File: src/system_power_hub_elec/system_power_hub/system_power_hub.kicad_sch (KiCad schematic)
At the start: 43 parts, among them J101 SM02B-PASS, J6 IDC6, U102 TCAN1462V, U2 STM32G474RBT6, U4 24LC128, Y1 24MHz

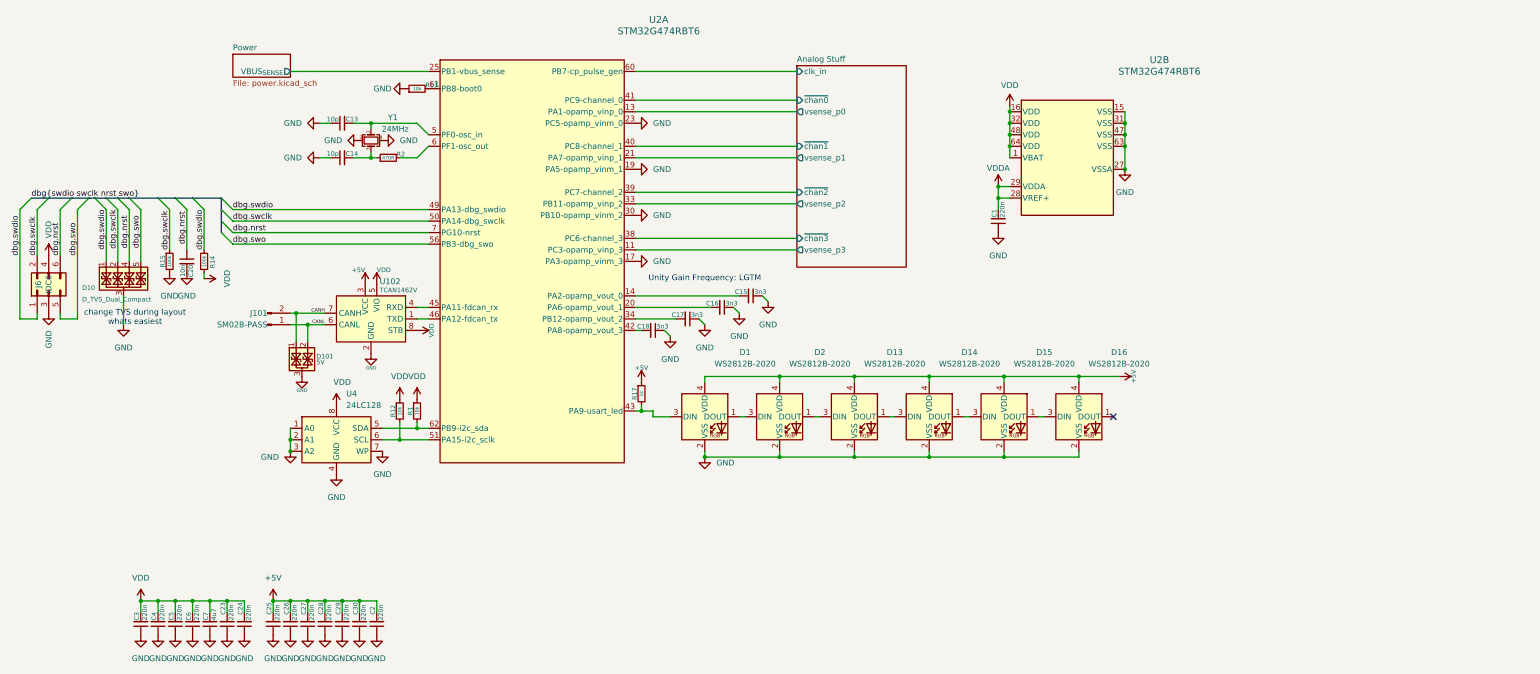
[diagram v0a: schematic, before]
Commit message: [WIP] Copied KiCAD proj from MPM, modified schematic for SPM
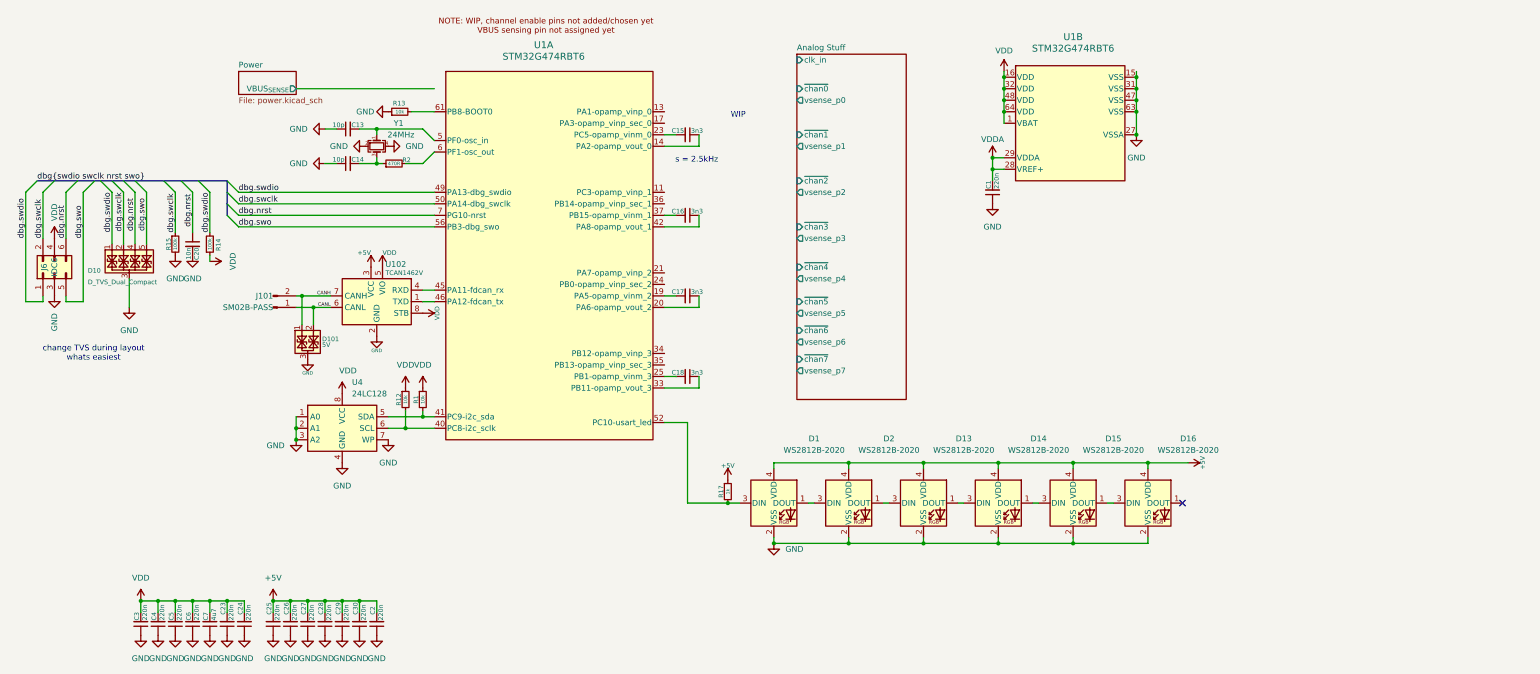
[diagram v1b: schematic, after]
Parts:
- removed U2: STM32G474RBT6, Package_QFP:LQFP-64_10x10mm_P0.5mm, symbol Main_Power_Module:STM32G474RBT6
- added U1: STM32G474RBT6, LQFP64-10x10mm, symbol CubeMX:STM32G474RBT6
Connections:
- net GND: now also U1.15 (VSS), U1.27 (VSSA), U1.31 (VSS), U1.47 (VSS), U1.63 (VSS); no longer C15.1, C16.1, C17.1, C18.1
- net VDD: now also U1.1 (VBAT), U1.16 (VDD), U1.32 (VDD), U1.48 (VDD), U1.64 (VDD)
- net VDDA: now also U1.28 (VREF+), U1.29 (VDDA)
- net dbg.nrst: now also U1.7 (PG10-nrst)
- net dbg.swclk: now also U1.50 (PA14-dbg_swclk)
- net dbg.swdio: now also U1.49 (PA13-dbg_swdio)
- net dbg.swo: now also U1.56 (PB3-dbg_swo)
- net at C15.2: now also U1.23 (PC5-opamp_vinm_0)
- net at C16.2: now also U1.37 (PB15-opamp_vinm_1)
- net at C17.2: now also U1.19 (PA5-opamp_vinm_2)
- net at C18.2: now also U1.25 (PB1-opamp_vinm_3)
- net at D1.3 (DIN), R17.2: now also U1.52 (PC10-usart_led)
- net at U102.4 (RXD): now also U1.45 (PA11-fdcan_rx)
- net at U102.1 (TXD): now also U1.46 (PA12-fdcan_tx)
- net at C13.2, Y1.1: now also U1.5 (PF0-osc_in)
- net at R12.2, U4.6 (SCL): now also U1.40 (PC8-i2c_sclk)
- net at R2.2: now also U1.6 (PF1-osc_out)
- net at R13.2: now also U1.61 (PB8-BOOT0)
- net at R1.2, U4.5 (SDA): now also U1.41 (PC9-i2c_sda)
- new net: C17.1, U1.20 (PA6-opamp_vout_2)
- new net: C15.1, U1.14 (PA2-opamp_vout_0)
- new net: C16.1, U1.42 (PA8-opamp_vout_1)
- new net: C18.1, U1.33 (PB11-opamp_vout_3)
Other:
- sheet Analog Stuff ports: added vsense_p4, vsense_p5, vsense_p6, vsense_p7, ~{chan4}, ~{chan5}, ~{chan6}, ~{chan7}; removed none
- note added: "WIP"
- note added: "s = 2.5kHz"
- note removed: "Unity Gain Frequency: LGTM"
- moved on the sheet: C1, C13, C14, C15, C16, C17, C18, C20, D1, D10, D101, D13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

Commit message: Draft SPM PCB layout
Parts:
- U1: footprint LQFP64-10x10mm -> Package_QFP:LQFP-64_10x10mm_P0.5mm
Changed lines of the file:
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@@
 			)
 		)
-		(property "Footprint" "LQFP64-10x10mm"
+		(property "Footprint" "Package_QFP:LQFP-64_10x10mm_P0.5mm"
 			(at 233.68 43.18 0)
 			(effects
@@
 			)
 		)
-		(property "Footprint" "LQFP64-10x10mm"
+		(property "Footprint" "Package_QFP:LQFP-64_10x10mm_P0.5mm"
 			(at 115.57 41.91 0)
 			(effects

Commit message: Draft layout done, need to continue routing and decide on GPIO
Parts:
- added C32, C33, C60, C61: 220n, Capacitor_SMD:C_0402_1005Metric, symbol Bluesat:C_CompactV
- added D4, D5, D6, D7: WS2812B-2020, LED_SMD:LED_WS2812B-2020_PLCC4_2.0x2.0mm, symbol LED:WS2812B-2020
- added H1, H2, H3, H4: MountingHole, Bluesat:M2.5, symbol Mechanical:MountingHole
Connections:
- net +5V: now also C32.2, C33.2, C60.2, C61.2, D4.4 (VDD), D5.4 (VDD), D6.4 (VDD), D7.4 (VDD)
- net GND: now also C32.1, C33.1, C60.1, C61.1, D4.2 (VSS), D5.2 (VSS), D6.2 (VSS), D7.2 (VSS)
- net at D16.1 (DOUT): now also D4.3 (DIN)
- new net: D5.1 (DOUT), D6.3 (DIN)
- new net: D4.1 (DOUT), D5.3 (DIN)
- new net: D6.1 (DOUT), D7.3 (DIN)

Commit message: More basic routing updates
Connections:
- net GND: now also U102.8 (STB)
- net VDD: no longer U102.8 (STB)
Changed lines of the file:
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@@
 	)
 	(junction
+		(at 100.33 100.33)
+		(diameter 0)
+		(color 0 0 0 0)
+	)
+	(junction
 		(at 204.47 128.27)
 		(diameter 0)
@@
 	(wire
 		(pts
+			(xy 110.49 95.25) (xy 110.49 100.33)
+		)
+		(stroke
+			(width 0)
+			(type default)
+		)
+	)
+	(wire
+		(pts
 			(xy 102.87 120.65) (xy 106.68 120.65)
 		)
@@
 		)
 	)
+	(wire
+		(pts
+			(xy 110.49 100.33) (xy 100.33 100.33)
+		)
+		(stroke
+			(width 0)
+			(type default)
+		)
+	)
 	(bus
 		(pts
@@
 					(unit 1)
 				)
-			)
-		)
-	)
-	(symbol
-		(lib_id "power:VDD")
-		(at 110.49 95.25 270)
-		(unit 1)
-		(exclude_from_sim no)
-		(in_bom yes)
-		(on_board yes)
-		(dnp no)
-		(property "Reference" "#PWR0122"
-			(at 106.68 95.25 0)
-			(effects
-				(font
-					(size 1.27 1.27)
-				)
-				(hide yes)
-			)
-		)
-		(property "Value" "VDD"
-			(at 113.665 95.25 0)
-			(effects
-				(font
-					(size 1.016 1.016)
-				)
-			)
-		)
-		(property "Footprint" ""
-			(at 110.49 95.25 0)
-			(effects
-				(font
-					(size 1.27 1.27)
-				)
-				(hide yes)
-			)
-		)
-		(property "Datasheet" ""
-			(at 110.49 95.25 0)
-			(effects
-				(font
-					(size 1.27 1.27)
-				)
-				(hide yes)
-			)
-		)
-		(property "Description" "Power symbol creates a global label with name \"VDD\""
-			(at 110.49 95.25 0)
-			(effects
-				(font
-					(size 1.27 1.27)
-				)
-				(hide yes)
-			)
-		)
-		(pin "1"
-		)
-		(instances
-			(project "main_power_hub"
-				(path "/535f321e-8428-4dab-8e55-8d6d7e9876bc"
-					(reference "#PWR0122")
-					(unit 1)
-				)

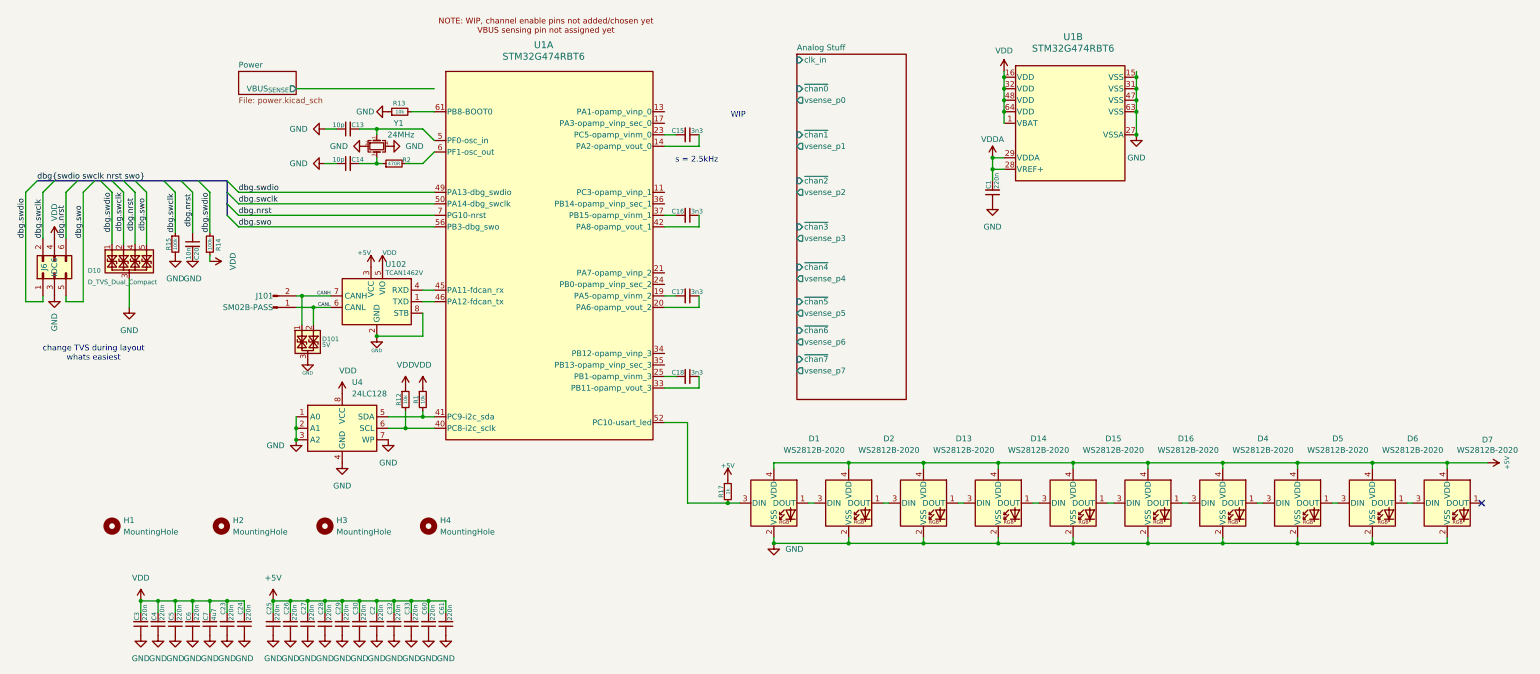
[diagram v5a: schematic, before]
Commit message: Completed channel wiring/routing, vbus sense routed
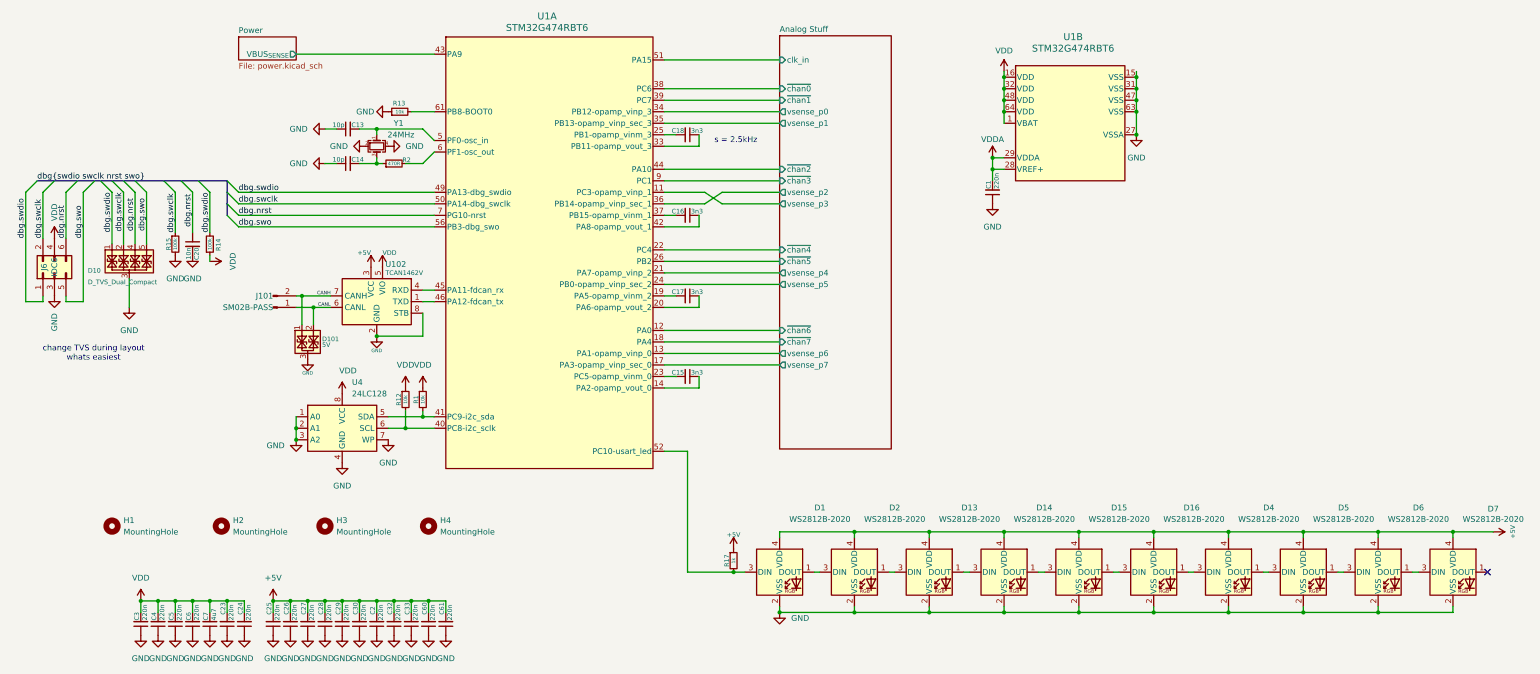
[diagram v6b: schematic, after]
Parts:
- U1: footprint Package_QFP:LQFP-64_10x10mm_P0.5mm -> LQFP64-10x10mm
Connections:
- net Analog Stuff/clk_in: now also U1.51 (PA15)
- net Analog Stuff/vsense_p0: now also U1.34 (PB12-opamp_vinp_3)
- net Analog Stuff/vsense_p1: now also U1.35 (PB13-opamp_vinp_sec_3)
- net Analog Stuff/vsense_p2: now also U1.36 (PB14-opamp_vinp_sec_1)
- net Analog Stuff/vsense_p3: now also U1.11 (PC3-opamp_vinp_1)
- net Analog Stuff/vsense_p4: now also U1.21 (PA7-opamp_vinp_2)
- net Analog Stuff/vsense_p5: now also U1.24 (PB0-opamp_vinp_sec_2)
- net Analog Stuff/vsense_p6: now also U1.13 (PA1-opamp_vinp_0)
- net Analog Stuff/vsense_p7: now also U1.17 (PA3-opamp_vinp_sec_0)
- net Analog Stuff/~{chan0}: now also U1.38 (PC6)
- net Analog Stuff/~{chan1}: now also U1.39 (PC7)
- net Analog Stuff/~{chan2}: now also U1.44 (PA10)
- net Analog Stuff/~{chan3}: now also U1.9 (PC1)
- net Analog Stuff/~{chan4}: now also U1.22 (PC4)
- net Analog Stuff/~{chan5}: now also U1.26 (PB2)
- net Analog Stuff/~{chan6}: now also U1.12 (PA0)
- net Analog Stuff/~{chan7}: now also U1.18 (PA4)
- net Power/VBUS_{SENSE}: now also U1.43 (PA9)
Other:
- note removed: "WIP"
- moved on the sheet: C15, C18, D1, D13, D14, D15, D16, D2, D4, D5, D6, D7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

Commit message: Fix SPM schematic as per errata 04-02-2026
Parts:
- H1, H2, H3, H4: footprint Bluesat:M2.5 -> Bluesat:M2.5_Internal
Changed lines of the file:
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@@
 			)
 		)
-		(property "Footprint" "Bluesat:M2.5"
+		(property "Footprint" "Bluesat:M2.5_Internal"
 			(at 66.04 142.24 0)
 			(effects
@@
 			)
 		)
-		(property "Footprint" "Bluesat:M2.5"
+		(property "Footprint" "Bluesat:M2.5_Internal"
 			(at 88.9 142.24 0)
 			(effects
@@
 			)
 		)
-		(property "Footprint" "Bluesat:M2.5"
+		(property "Footprint" "Bluesat:M2.5_Internal"
 			(at 111.76 142.24 0)
 			(effects
@@
 			)
 		)
-		(property "Footprint" "Bluesat:M2.5"
+		(property "Footprint" "Bluesat:M2.5_Internal"
 			(at 41.91 142.24 0)
 			(effects

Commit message: Cleaned up routing and adjusted PCB layout
- Moved components at least 1.5mm away from board edge
- Adjusted board size slightly for more clearance
- Removed pullups for eeprom
- Adjusted via sizing, made some smaller
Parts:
- removed R1, R12: 10k, Resistor_SMD:R_0402_1005Metric, symbol Bluesat:R_CompactV
- added C11: 220n, Capacitor_SMD:C_0402_1005Metric, symbol Bluesat:C_CompactV
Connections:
- net GND: now also C11.1
- net VDD: now also C11.2
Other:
- moved on the sheet: C23, C24, C3, C4, C5, C6, C7
